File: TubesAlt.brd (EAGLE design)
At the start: 100 x 80 mm, 46 parts, among them T0 MPSA42, T1 MPSA42, T10 MPSA42, T11 MPSA42, T12 MPSA42, T13 MPSA42, T14 MPSA42, T15 MPSA42, T16 MPSA42, T17 MPSA42, T18 MPSA42, T19 MPSA42, T2 MPSA42, T3 MPSA42, T4 MPSA42, T5 MPSA42, T6 MPSA42, T7 MPSA42, T8 MPSA42, T9 MPSA42

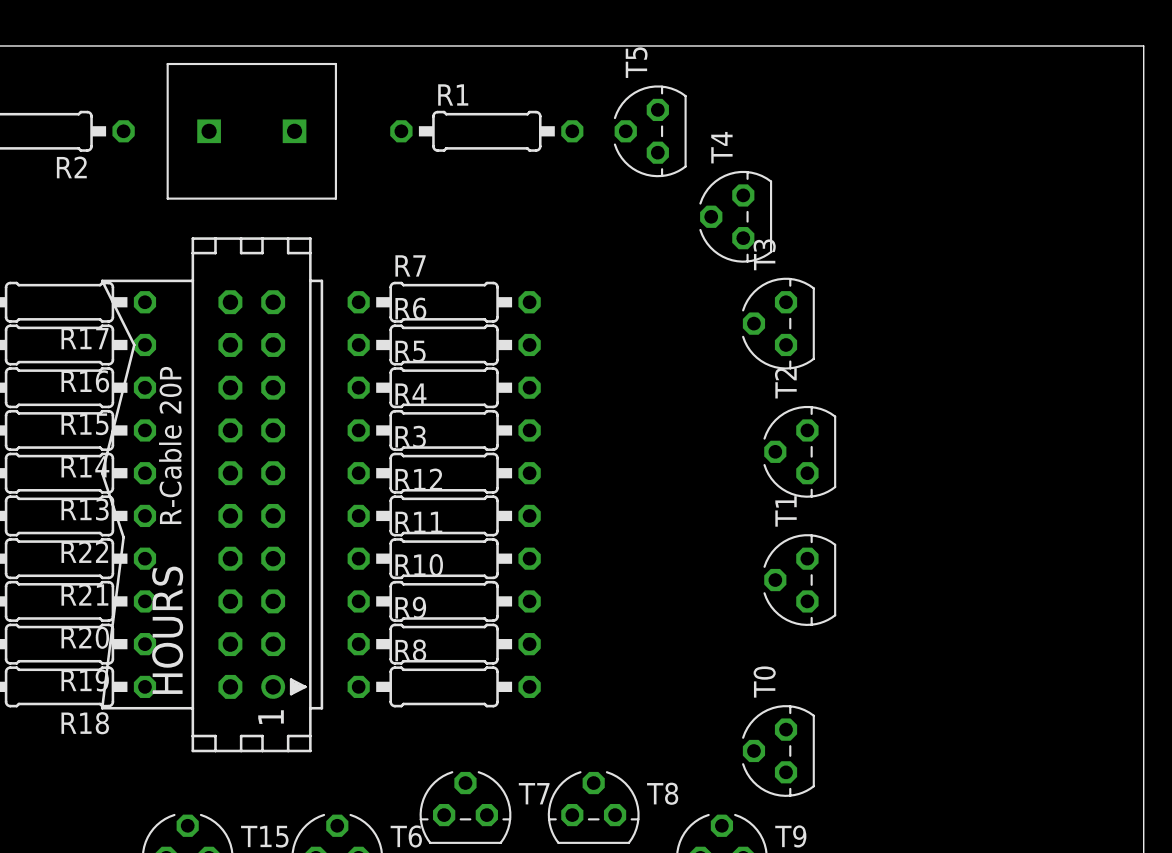
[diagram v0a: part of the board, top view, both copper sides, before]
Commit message: Add TubeAlt, rename Control Logic, use jumper
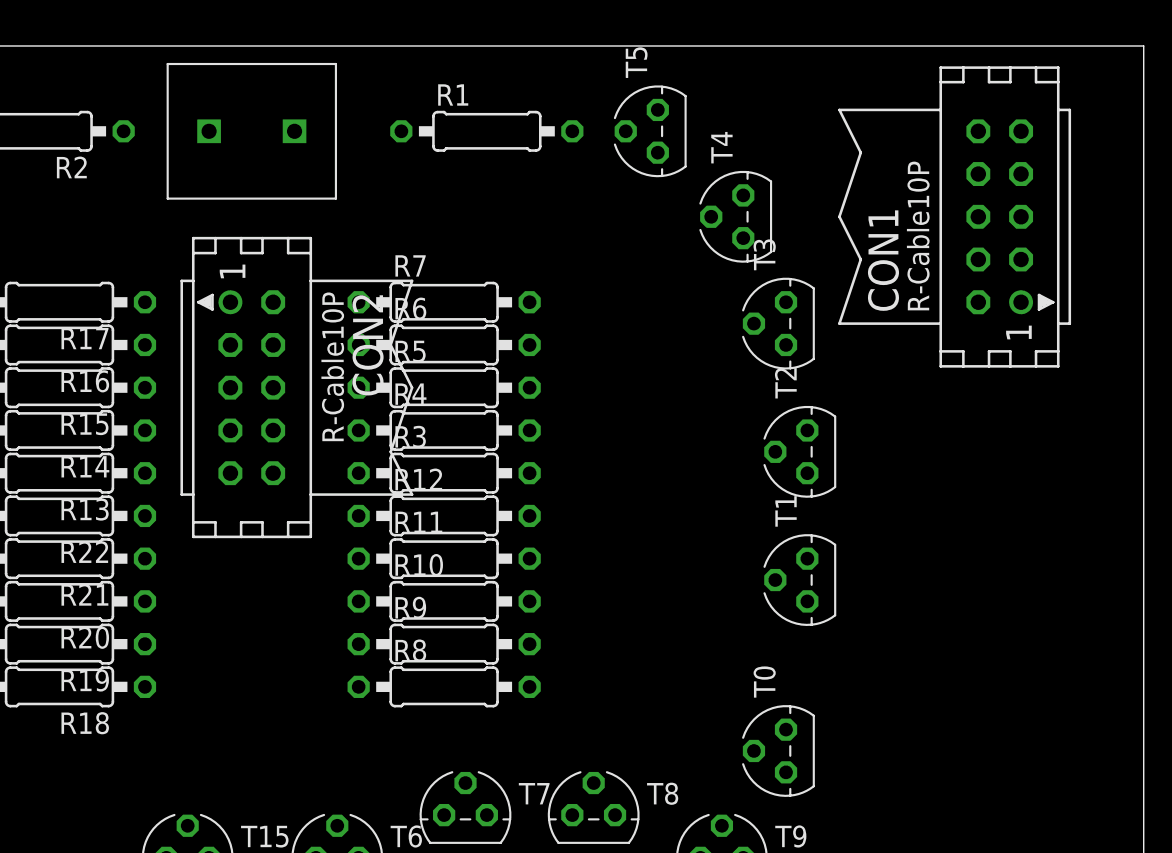
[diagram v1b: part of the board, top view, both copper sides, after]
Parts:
- removed HOURS: (no value), con-harting:CON20
- added CON1, CON2: (no value), con-harting:CON10
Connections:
- net DIGIT_D0: no longer HOURS.10
- net DIGIT_D1: now also CON2.10; no longer HOURS.12
- net DIGIT_D2: now also CON2.8; no longer HOURS.14
- net DIGIT_D3: now also CON2.6; no longer HOURS.16
- net DIGIT_D4: now also CON2.4; no longer HOURS.18
- net DIGIT_D5: now also CON2.2; no longer HOURS.20
- net DIGIT_D6: no longer HOURS.2
- net DIGIT_D7: no longer HOURS.4
- net DIGIT_D8: no longer HOURS.6
- net DIGIT_D9: no longer HOURS.8
- net DIGIT_U0: no longer HOURS.9
- net DIGIT_U1: now also CON1.10; no longer HOURS.11
- net DIGIT_U2: now also CON1.8; no longer HOURS.13
- net DIGIT_U3: now also CON1.6; no longer HOURS.15
- net DIGIT_U4: now also CON1.4; no longer HOURS.17
- net DIGIT_U5: now also CON1.2; no longer HOURS.19
- net DIGIT_U6: no longer HOURS.1
- net DIGIT_U7: no longer HOURS.3
- net DIGIT_U8: no longer HOURS.5
- net DIGIT_U9: no longer HOURS.7
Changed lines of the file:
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@@
 </autorouter>
 <elements>
-<element name="HOURS" library="con-harting" package="CON20" value="" x="46.99" y="53.34" rot="R90">
-<attribute name="OC_FARNELL" value="unknown" x="46.99" y="53.34" size="1.778" layer="27" rot="R90" display="off"/>
-<attribute name="OC_NEWARK" value="unknown" x="46.99" y="53.34" size="1.778" layer="27" rot="R90" display="off"/>
-<attribute name="MF" value="" x="46.99" y="53.34" size="1.778" layer="27" rot="R90" display="off"/>
-<attribute name="MPN" value="" x="46.99" y="53.34" size="1.778" layer="27" rot="R90" display="off"/>
-</element>
 <element name="HOURS_U" library="russian-nixies" package="IN-14" value="IN-14" x="63.5" y="21.59" rot="R180"/>
 <element name="POWER_SUPPLY" library="PGT" package="SIL_2_0.2INCH" value="CON_2_SIL" x="46.99" y="74.93" rot="R270"/>
@@
 <element name="R21" library="resistor" package="0207/10" value="" x="35.56" y="49.53" rot="R180"/>
 <element name="R22" library="resistor" package="0207/10" value="" x="35.56" y="52.07" rot="R180"/>
+<element name="CON1" library="con-harting" package="CON10" value="" x="91.44" y="69.85" rot="R90">
+<attribute name="OC_FARNELL" value="unknown" x="91.44" y="69.85" size="1.778" layer="27" rot="R90" display="off"/>
+<attribute name="MF" value="" x="91.44" y="69.85" size="1.778" layer="27" rot="R90" display="off"/>
+<attribute name="OC_NEWARK" value="unknown" x="91.44" y="69.85" size="1.778" layer="27" rot="R90" display="off"/>
+<attribute name="MPN" value="" x="91.44" y="69.85" size="1.778" layer="27" rot="R90" display="off"/>
+</element>
+<element name="CON2" library="con-harting" package="CON10" value="" x="46.99" y="59.69" rot="R270">
+<attribute name="OC_FARNELL" value="unknown" x="46.99" y="59.69" size="1.778" layer="27" rot="R270" display="off"/>
+<attribute name="MF" value="" x="46.99" y="59.69" size="1.778" layer="27" rot="R270" display="off"/>
+<attribute name="OC_NEWARK" value="unknown" x="46.99" y="59.69" size="1.778" layer="27" rot="R270" display="off"/>
+<attribute name="MPN" value="" x="46.99" y="59.69" size="1.778" layer="27" rot="R270" display="off"/>
+</element>
 </elements>
 <signals>
@@
 <signal name="DIGIT_U1">
 <contactref element="R3" pad="1"/>
-<contactref element="HOURS" pad="11"/>
-<wire x1="48.26" y1="54.61" x2="53.34" y2="54.61" width="0" layer="19" extent="1-1"/>
+<contactref element="CON1" pad="10"/>
+<wire x1="90.17" y1="74.93" x2="53.34" y2="54.61" width="0" layer="19" extent="1-1"/>
 </signal>
 <signal name="DIGIT_U2">
 <contactref element="R4" pad="1"/>
-<contactref element="HOURS" pad="13"/>
-<wire x1="48.26" y1="57.15" x2="53.34" y2="57.15" width="0" layer="19" extent="1-1"/>
+<contactref element="CON1" pad="8"/>
+<wire x1="90.17" y1="72.39" x2="53.34" y2="57.15" width="0" layer="19" extent="1-1"/>
 </signal>
 <signal name="DIGIT_U3">
 <contactref element="R5" pad="1"/>
-<contactref element="HOURS" pad="15"/>
-<wire x1="48.26" y1="59.69" x2="53.34" y2="59.69" width="0" layer="19" extent="1-1"/>
+<contactref element="CON1" pad="6"/>
+<wire x1="90.17" y1="69.85" x2="53.34" y2="59.69" width="0" layer="19" extent="1-1"/>
 </signal>
 <signal name="DIGIT_U4">
 <contactref element="R6" pad="1"/>
-<contactref element="HOURS" pad="17"/>
-<wire x1="48.26" y1="62.23" x2="53.34" y2="62.23" width="0" layer="19" extent="1-1"/>
+<contactref element="CON1" pad="4"/>
+<wire x1="90.17" y1="67.31" x2="53.34" y2="62.23" width="0" layer="19" extent="1-1"/>
 </signal>
 <signal name="DIGIT_U5">
 <contactref element="R7" pad="1"/>
-<contactref element="HOURS" pad="19"/>
-<wire x1="48.26" y1="64.77" x2="53.34" y2="64.77" width="0" layer="19" extent="1-1"/>
+<contactref element="CON1" pad="2"/>
+<wire x1="90.17" y1="64.77" x2="53.34" y2="64.77" width="0" layer="19" extent="1-1"/>
 </signal>
 <signal name="DIGIT_U6">
 <contactref element="R8" pad="1"/>
-<contactref element="HOURS" pad="1"/>
-<wire x1="48.26" y1="41.91" x2="53.34" y2="41.91" width="0" layer="19" extent="1-1"/>
 </signal>
 <signal name="DIGIT_U8">
 <contactref element="R10" pad="1"/>
-<contactref element="HOURS" pad="5"/>
-<wire x1="48.26" y1="46.99" x2="53.34" y2="46.99" width="0" layer="19" extent="1-1"/>
 </signal>
 <signal name="DIGIT_U9">
 <contactref element="R11" pad="1"/>
-<contactref element="HOURS" pad="7"/>
-<wire x1="48.26" y1="49.53" x2="53.34" y2="49.53" width="0" layer="19" extent="1-1"/>
 </signal>
 <signal name="DIGIT_U0">
 <contactref element="R12" pad="1"/>
-<contactref element="HOURS" pad="9"/>
-<wire x1="48.26" y1="52.07" x2="53.34" y2="52.07" width="0" layer="19" extent="1-1"/>
 </signal>
 <signal name="DIGIT_U7">
 <contactref element="R9" pad="1"/>
-<contactref element="HOURS" pad="3"/>
-<wire x1="48.26" y1="44.45" x2="53.34" y2="44.45" width="0" layer="19" extent="1-1"/>
 </signal>
 <signal name="N$17">
@@
 <signal name="DIGIT_D1">
 <contactref element="R13" pad="1"/>
-<contactref element="HOURS" pad="12"/>
-<wire x1="40.64" y1="54.61" x2="45.72" y2="54.61" width="0" layer="19" extent="1-1"/>
+<contactref element="CON2" pad="10"/>
+<wire x1="48.26" y1="54.61" x2="40.64" y2="54.61" width="0" layer="19" extent="1-1"/>
 </signal>
 <signal name="DIGIT_D2">
 <contactref element="R14" pad="1"/>
-<contactref element="HOURS" pad="14"/>
-<wire x1="40.64" y1="57.15" x2="45.72" y2="57.15" width="0" layer="19" extent="1-1"/>
+<contactref element="CON2" pad="8"/>
+<wire x1="48.26" y1="57.15" x2="40.64" y2="57.15" width="0" layer="19" extent="1-1"/>
 </signal>
 <signal name="DIGIT_D3">
 <contactref element="R15" pad="1"/>
-<contactref element="HOURS" pad="16"/>
-<wire x1="40.64" y1="59.69" x2="45.72" y2="59.69" width="0" layer="19" extent="1-1"/>
+<contactref element="CON2" pad="6"/>
+<wire x1="48.26" y1="59.69" x2="40.64" y2="59.69" width="0" layer="19" extent="1-1"/>
 </signal>
 <signal name="DIGIT_D4">
 <contactref element="R16" pad="1"/>
-<contactref element="HOURS" pad="18"/>
-<wire x1="40.64" y1="62.23" x2="45.72" y2="62.23" width="0" layer="19" extent="1-1"/>
+<contactref element="CON2" pad="4"/>
+<wire x1="48.26" y1="62.23" x2="40.64" y2="62.23" width="0" layer="19" extent="1-1"/>
 </signal>
 <signal name="DIGIT_D5">
 <contactref element="R17" pad="1"/>
-<contactref element="HOURS" pad="20"/>
-<wire x1="40.64" y1="64.77" x2="45.72" y2="64.77" width="0" layer="19" extent="1-1"/>
+<contactref element="CON2" pad="2"/>
+<wire x1="48.26" y1="64.77" x2="40.64" y2="64.77" width="0" layer="19" extent="1-1"/>
 </signal>
 <signal name="DIGIT_D6">
 <contactref element="R18" pad="1"/>
-<contactref element="HOURS" pad="2"/>
-<wire x1="40.64" y1="41.91" x2="45.72" y2="41.91" width="0" layer="19" extent="1-1"/>
 </signal>
 <signal name="DIGIT_D7">
 <contactref element="R19" pad="1"/>
-<contactref element="HOURS" pad="4"/>
-<wire x1="40.64" y1="44.45" x2="45.72" y2="44.45" width="0" layer="19" extent="1-1"/>
 </signal>
 <signal name="DIGIT_D8">
 <contactref element="R20" pad="1"/>
-<contactref element="HOURS" pad="6"/>
-<wire x1="40.64" y1="46.99" x2="45.72" y2="46.99" width="0" layer="19" extent="1-1"/>
 </signal>
 <signal name="DIGIT_D9">
 <contactref element="R21" pad="1"/>
-<contactref element="HOURS" pad="8"/>
-<wire x1="40.64" y1="49.53" x2="45.72" y2="49.53" width="0" layer="19" extent="1-1"/>
 </signal>
 <signal name="DIGIT_D0">
 <contactref element="R22" pad="1"/>
-<contactref element="HOURS" pad="10"/>
-<wire x1="40.64" y1="52.07" x2="45.72" y2="52.07" width="0" layer="19" extent="1-1"/>
 </signal>
 </signals>
